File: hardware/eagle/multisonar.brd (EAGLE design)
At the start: 96 x 96 mm, 21 parts, among them IC1 ATMEGA328-20P, J1 ARDUINO_R3_SHIELD, Y1 16MHZ

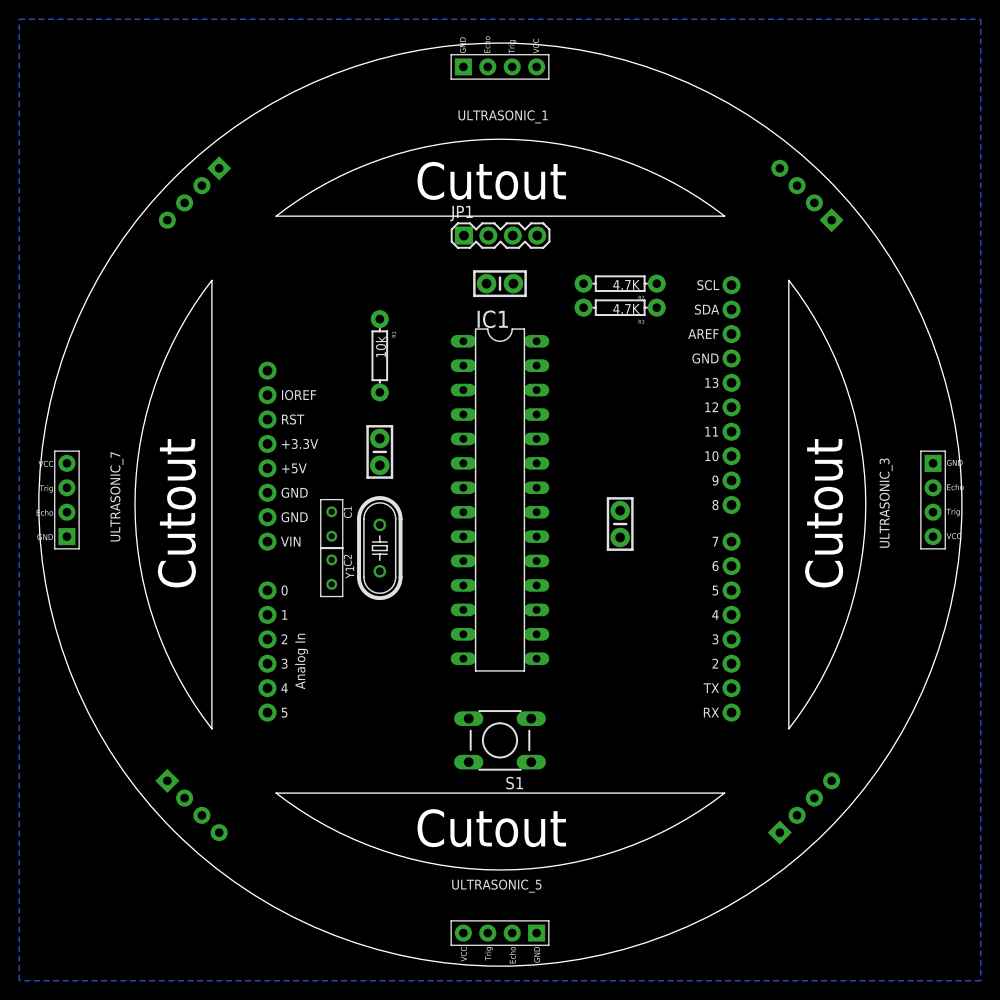
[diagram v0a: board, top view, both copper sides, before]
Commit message: Routed power lines
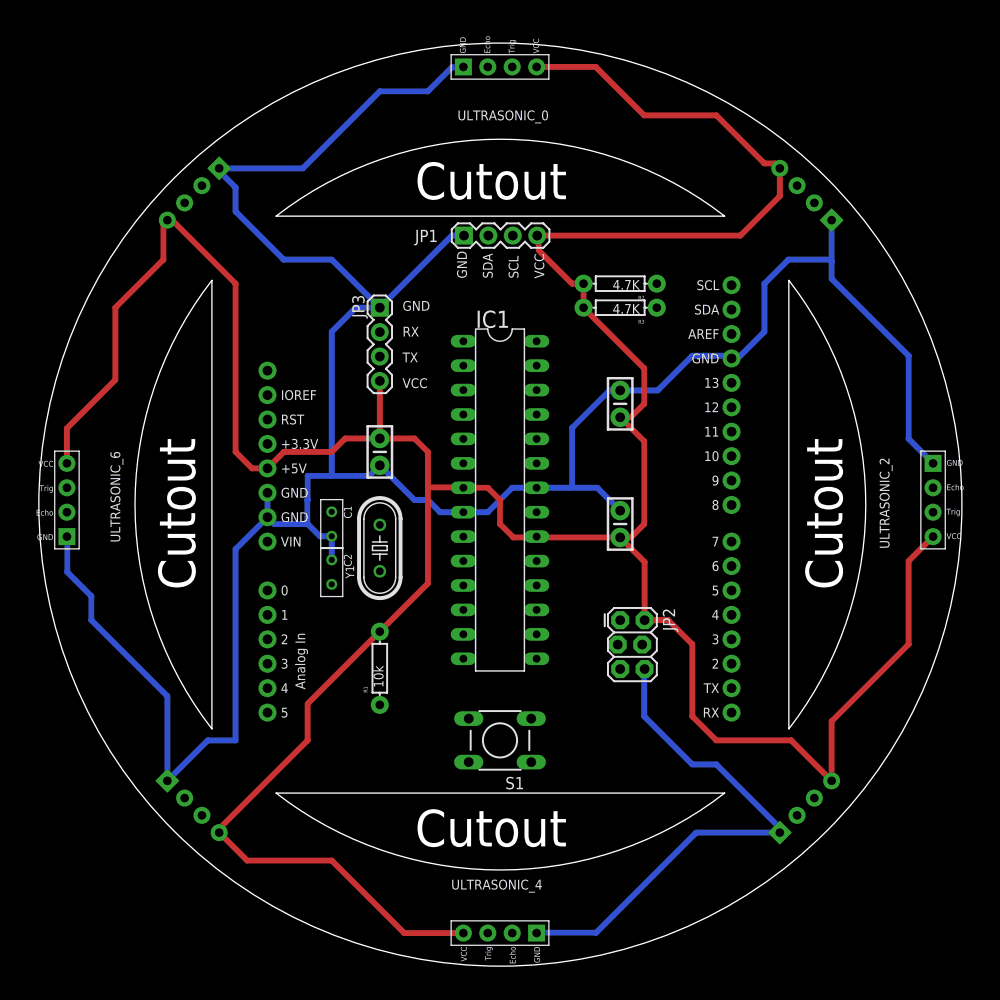
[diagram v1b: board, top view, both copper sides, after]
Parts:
- removed ULTRASONIC_8: HC-SR04, Ultrasonic Sensor HC-SR04:HC-SR04_FOOTPRINT
- added JP2: ICSP, SparkFun-Connectors:2X3_LOCK
- added JP3: (no value), SparkFun-Connectors:1X04
- added ULTRASONIC_0: HC-SR04, Ultrasonic Sensor HC-SR04:HC-SR04_FOOTPRINT
- moved ULTRASONIC_3 32.6 mm to (112.5, 19.9), flipped to the bottom, turned to 225 degrees
- moved ULTRASONIC_6 32.6 mm to (40.0, 50.0), flipped to the top, turned to 180 degrees
- moved ULTRASONIC_5 32.6 mm to (52.4, 19.9), flipped to the bottom, turned to 315 degrees
- moved R1 32.5 mm to (70.0, 32.5), turned to 90 degrees
- moved ULTRASONIC_1 32.5 mm to (112.5, 80.0), flipped to the bottom, turned to 135 degrees
- moved ULTRASONIC_2 32.5 mm to (125.0, 50.0), flipped to the top, turned to 0 degrees
- moved ULTRASONIC_7 32.5 mm to (52.4, 80.0), flipped to the bottom, turned to 45 degrees
- moved ULTRASONIC_4 32.5 mm to (82.5, 7.50), flipped to the top, turned to 270 degrees
- moved C5 17.7 mm to (95.0, 60.0), turned to 270 degrees
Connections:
- removed net N$1: IC1.1, R1.P$1, S1.3
- new net PB0: IC1.14, ULTRASONIC_5.ECHO
- new net PB1: IC1.15, ULTRASONIC_5.TRIG
- new net PB2: IC1.16, ULTRASONIC_6.ECHO
- new net PB3: IC1.17, JP2.4, ULTRASONIC_6.TRIG
- new net PB4: IC1.18, JP2.1, ULTRASONIC_7.ECHO
- new net PB5: IC1.19, JP2.3, ULTRASONIC_7.TRIG
- new net PC0: IC1.23, ULTRASONIC_0.ECHO
- new net PC1: IC1.24, ULTRASONIC_0.TRIG
- new net PC2: IC1.25, ULTRASONIC_1.ECHO
- new net PC3: IC1.26, ULTRASONIC_1.TRIG
- new net PD2: IC1.4, ULTRASONIC_2.ECHO
- new net PD3: IC1.5, ULTRASONIC_2.TRIG
- new net PD4: IC1.6, ULTRASONIC_3.ECHO
- new net PD5: IC1.11, ULTRASONIC_3.TRIG
- new net PD6: IC1.12, ULTRASONIC_4.ECHO
- new net PD7: IC1.13, ULTRASONIC_4.TRIG
- new net RST: IC1.1, JP2.5, R1.P$1, S1.3
- new net RX: IC1.2, JP3.2
- new net TX: IC1.3, JP3.3
- net GND: now also JP2.6, JP3.1, ULTRASONIC_0.GND, ULTRASONIC_1.GND, ULTRASONIC_2.GND, ULTRASONIC_3.GND, ULTRASONIC_4.GND, ULTRASONIC_5.GND, ULTRASONIC_6.GND, ULTRASONIC_7.GND
- net VCC: now also JP2.2, JP3.4, ULTRASONIC_0.VCC, ULTRASONIC_1.VCC, ULTRASONIC_2.VCC, ULTRASONIC_3.VCC, ULTRASONIC_4.VCC, ULTRASONIC_5.VCC, ULTRASONIC_6.VCC, ULTRASONIC_7.VCC
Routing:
- net VCC: track 0.00 -> 358.4 mm
- net GND: track 0.00 -> 332.2 mm
- removed copper zone on layer 16, net GND
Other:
- board text added: "GND"
- board text added: "RX"
- board text added: "SCL"
- board text added: "SDA"
- board text added: "TX"
- board text added: "VCC"
